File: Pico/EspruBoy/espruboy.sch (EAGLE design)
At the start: 15 parts, among them J1 JST-2P-SMD-PW-3410050P1

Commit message: make tab big enough for LCD
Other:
- note added: "TODO: Bigger holes for supercap Move ESP8266 module over to avoid tab of LCD"
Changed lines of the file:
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@@
 <sheet>
 <plain>
+<text x="81.28" y="78.74" size="1.778" layer="91">TODO:
+Bigger holes for supercap
+Move ESP8266 module over to avoid tab of LCD</text>
 </plain>
 <instances>

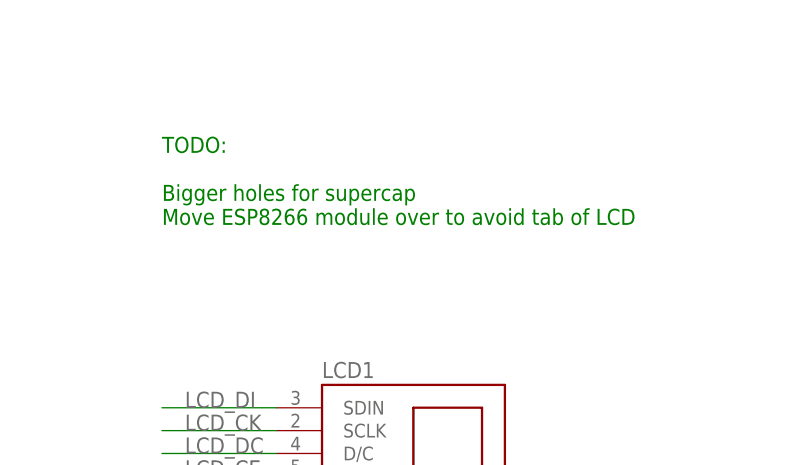
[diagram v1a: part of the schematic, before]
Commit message: fix shorted cr2032 battery connection
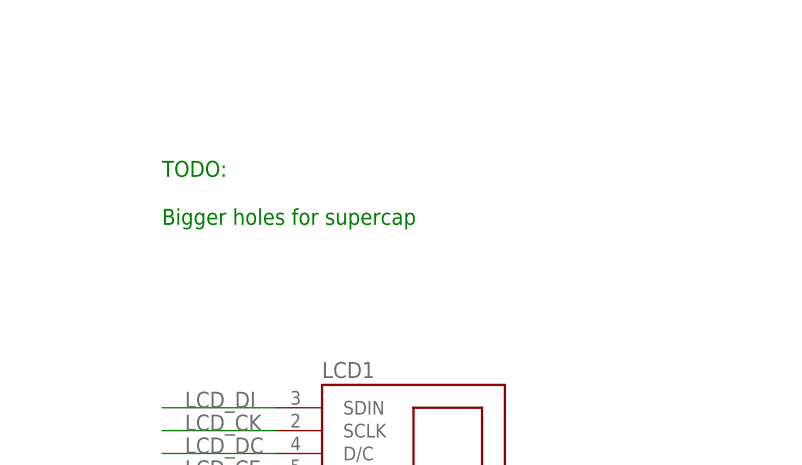
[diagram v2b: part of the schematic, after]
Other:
- note added: "TODO: Bigger holes for supercap"
- note removed: "TODO: Bigger holes for supercap Move ESP8266 module over to avoid tab of LCD"
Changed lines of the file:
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@@
 <text x="81.28" y="78.74" size="1.778" layer="91">TODO:
 Bigger holes for supercap
-Move ESP8266 module over to avoid tab of LCD</text>
+</text>
 </plain>
 <instances>
